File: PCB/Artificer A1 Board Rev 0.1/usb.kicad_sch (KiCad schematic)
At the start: 24 parts, among them U20 GT-USB-7010ASV, U21 CH217K, U22 CH334F_C5187527, U23 CH217K, X3 SMD-3225_4P12M12PF10PPM

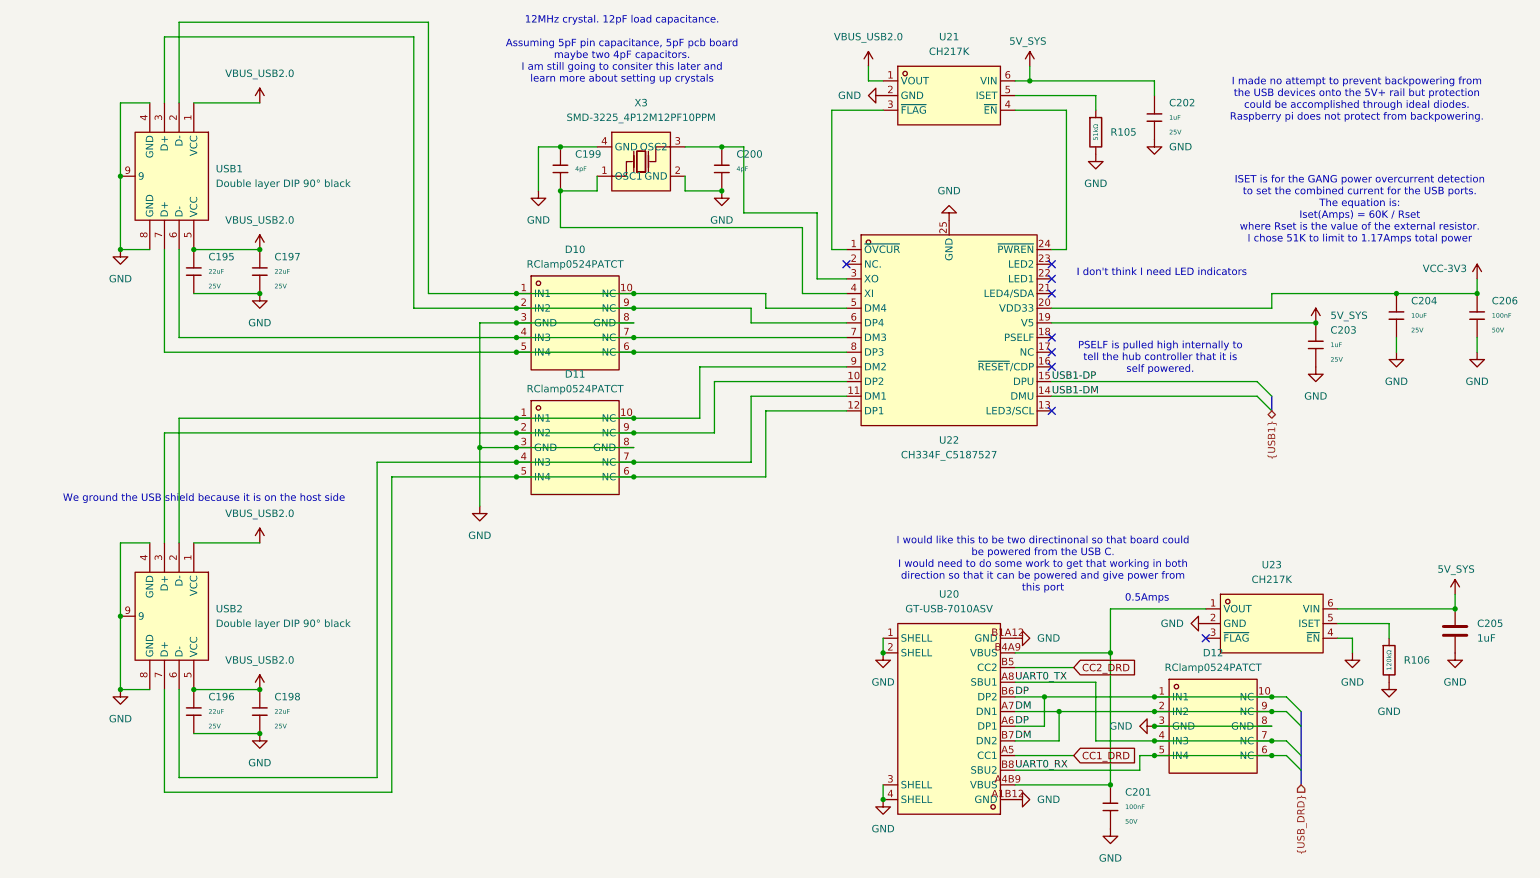
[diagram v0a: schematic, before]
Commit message: placed all components
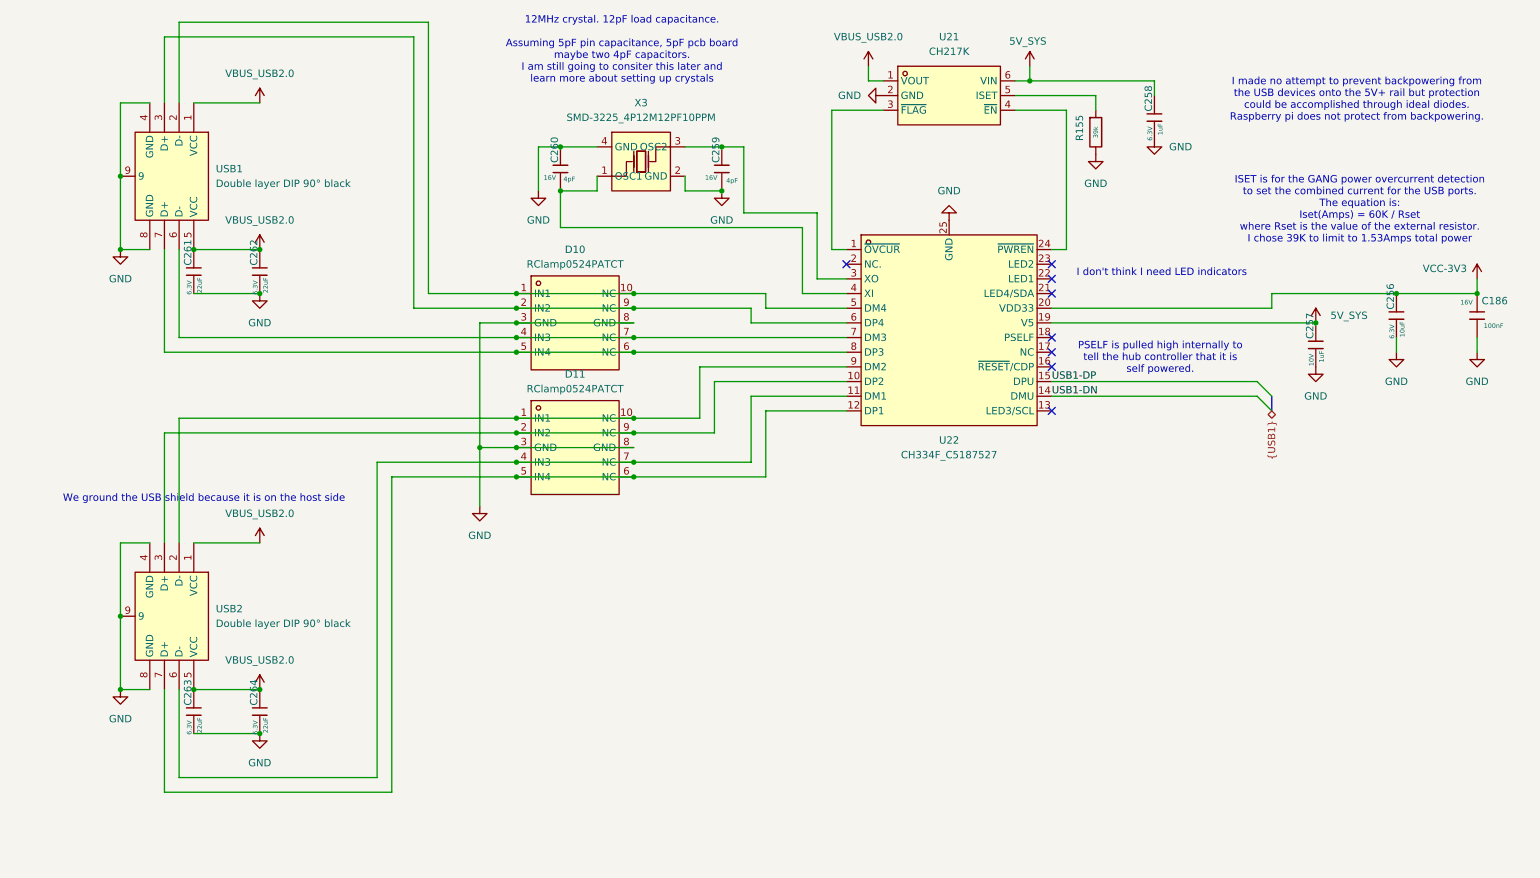
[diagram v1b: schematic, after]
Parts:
- removed C195, C196, C197, C198: 22uF, PCM_JLCPCB:C_0805, symbol PCM_JLCPCB-Capacitors:0805,22uF
- removed C199, C200: 4pF, PCM_JLCPCB:C_0402, symbol PCM_JLCPCB-Capacitors:0402,10pF
- removed C201, C206: 100nF, PCM_JLCPCB:C_0402, symbol PCM_JLCPCB-Capacitors:0402,100nF,(2)
- removed C202, C203: 1uF, PCM_JLCPCB:C_0402, symbol PCM_JLCPCB-Capacitors:0402,1uF
- removed C204: 10uF, PCM_JLCPCB:C_0603, symbol PCM_JLCPCB-Capacitors:0603,10uF,(2)
- removed C205: 1uF, symbol Device:C
- removed D12: RClamp0524PATCT, easyeda:SLP2510P8_L2.5-W1.0-P0.50-BL, symbol easyeda:RClamp0524PATCT
- removed R105: 51kΩ, PCM_JLCPCB:R_0402, symbol PCM_JLCPCB-Resistors:0402,51kΩ
- removed R106: 120kΩ, PCM_JLCPCB:R_0402, symbol PCM_JLCPCB-Resistors:0402,120kΩ
- removed U20: GT-USB-7010ASV, easyeda:USB-C-SMD_G-SWITCH_GT-USB-7010ASV, symbol easyeda:GT-USB-7010ASV
- removed U23: CH217K, easyeda:SOT-23-6_L2.9-W1.6-P0.95-LS2.8-BL, symbol easyeda:CH217K
- added C186: 100nF, Capacitor_SMD:C_0201_0603Metric, symbol Cap:JLCPCB_Lib_Blank_Cap
- added C256: 10uF, Capacitor_SMD:C_0402_1005Metric, symbol Cap:JLCPCB_Lib_Blank_Cap
- added C257: 1uF, Capacitor_SMD:C_0201_0603Metric, symbol Cap:JLCPCB_Lib_Blank_Cap
- added C258: 1uF, Capacitor_SMD:C_0402_1005Metric, symbol Cap:JLCPCB_Lib_Blank_Cap
- added C259, C260: 4pF, Capacitor_SMD:C_0201_0603Metric, symbol Cap:JLCPCB_Lib_Blank_Cap
- added C261, C262, C263, C264: 22uF, Capacitor_SMD:C_0603_1608Metric, symbol Cap:JLCPCB_Lib_Blank_Cap
- added R155: 39k, Resistor_SMD:R_0201_0603Metric, symbol Cap:JLCPCB_Res_Custom
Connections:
- net 5V_SYS: now also C257.2, C258.2
- net GND: now also C186.1, C256.1, C257.1, C258.1, C259.1, C260.2, C261.1, C262.1, C263.1, C264.1, R155.2
- net VBUS_USB2.0: now also C261.2, C262.2, C263.2, C264.2
- net VCC-3V3: now also C186.2, C256.2
- net at U22.3 (XO), X3.3 (OSC2): now also C259.2
- net at U22.4 (XI), X3.1 (OSC1): now also C260.1
- net at U21.5 (ISET): now also R155.1
- net USB1-DM renamed USB1-DN
- no-connect marks 9 -> 8
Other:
- note added: "ISET is for the GANG power overcurrent detection to set the combined current for the USB ports. The equation is: Iset(Amps) = 60K / Rset where Rset is the value of the external resistor. I chose 39K to limit to 1.53Amps total power"
- note removed: "0.5Amps"
- note removed: "I would like this to be two directinonal so that board could be powered from the USB C. I would need to do some work to get that working in both direction so that it can be powered and give power from this port"
- note removed: "ISET is for the GANG power overcurrent detection to set the combined current for the USB ports. The equation is: Iset(Amps) = 60K / Rset where Rset is the value of the external resistor. I chose 51K to limit to 1.17Amps total power"

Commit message: started routing
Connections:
- net USB2.0-2_DN: now reaches D11.1 (IN1), D11.10 (NC), U22.9 (DM2), USB2.2 (D-)
- net USB2.0-2_DP: now reaches D11.2 (IN2), D11.9 (NC), U22.10 (DP2), USB2.3 (D+)
- net USB2.0-1_DN: now reaches D11.4 (IN3), D11.7 (NC), U22.11 (DM1), USB2.6 (D-)
- net USB2.0-1_DP: now reaches D11.5 (IN4), D11.6 (NC), U22.12 (DP1), USB2.7 (D+)
- net USB2.0-4_DN: now reaches D10.1 (IN1), D10.10 (NC), U22.5 (DM4), USB1.2 (D-)
- net USB2.0-4_DP: now reaches D10.2 (IN2), D10.9 (NC), U22.6 (DP4), USB1.3 (D+)
- net USB2.0-3_DP: now reaches D10.4 (IN3), D10.7 (NC), U22.7 (DM3), USB1.6 (D-)
- net USB2.0-3_DN: now reaches D10.5 (IN4), D10.6 (NC), U22.8 (DP3), USB1.7 (D+)
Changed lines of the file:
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@@
+		)
+	)
+	(label "USB2.0-3_DN"
+		(at 67.31 73.66 0)
+		(effects
+			(font
+				(size 1.27 1.27)
+			)
+			(justify left bottom)
 		)
 	)
@@
 		(effects
 			(font
+				(size 1.27 1.27)
+			)
+			(justify left bottom)
+		)
+	)
+	(label "USB2.0-4_DP"
+		(at 83.82 40.64 90)
+		(effects
+			(font
+				(size 1.27 1.27)
+			)
+			(justify left bottom)
+		)
+	)
+	(label "USB2.0-1_DP"
+		(at 80.01 113.03 90)
+		(effects
+			(font
+				(size 1.27 1.27)
+			)
+			(justify left bottom)
+		)
+	)
+	(label "USB2.0-2_DP"
+		(at 69.85 87.63 0)
+		(effects
+			(font
+				(size 1.27 1.27)
+			)
+			(justify left bottom)
+		)
+	)
+	(label "USB2.0-1_DN"
+		(at 77.47 113.03 90)
+		(effects
+			(font
+				(size 1.27 1.27)
+			)
+			(justify left bottom)
+		)
+	)
+	(label "USB2.0-3_DP"
+		(at 67.31 71.12 0)
+		(effects
+			(font
+				(size 1.27 1.27)
+			)
+			(justify left bottom)
+		)
+	)
+	(label "USB2.0-2_DN"
+		(at 69.85 85.09 0)
+		(effects
+			(font
+				(size 1.27 1.27)
+			)
+			(justify left bottom)
+		)
+	)
+	(label "USB2.0-4_DN"
+		(at 86.36 40.64 90)
+		(effects
+			(font
